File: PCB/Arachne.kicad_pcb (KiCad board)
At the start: 2 copper layers, 100 x 100 mm, 276 parts, among them J201 SW2, J301 SW2, J401 SW2, J501 SW2, J601 SW2, J701 SW2, J801 V_IN, J901 USB_B, J902 PROG_CONN_STM_6p, J903 DBG_UART, M201 Stepper_Motor_bipolar, M301 Stepper_Motor_bipolar, M401 Stepper_Motor_bipolar, M501 Stepper_Motor_bipolar, M601 Stepper_Motor_bipolar, M701 Stepper_Motor_bipolar, Q801 AOD4189, SW101 SW_Push, U101 STM32L452CEUx, U102 WS2818B, U201 L6470_HTSSOP28, U301 L6470_HTSSOP28, U401 L6470_HTSSOP28, U501 L6470_HTSSOP28, U601 L6470_HTSSOP28, U701 L6470_HTSSOP28, U801 ACS712xLCTR-20A, U802 NCP1117-5.0_SOT223, U803 L5973D, U804 NCP1117-3.3_SOT223, U901 USBLC6-2SC6

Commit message: PCB: component sorting, add driver space marks to comment layer
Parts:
- moved J903 174.8 mm to (192.0, 60.0)
- moved U101 169.4 mm to (150.0, 73.0)
- moved C708 117.1 mm to (219.0, 153.0)
- moved R701 117.0 mm to (219.0, 143.0)
- moved C704 116.5 mm to (228.0, 143.0)
- moved C712 114.7 mm to (219.0, 148.0)
- moved R705 114.6 mm to (228.0, 148.0)
- moved C701 112.7 mm to (228.0, 153.0)
- moved C706 110.9 mm to (238.0, 143.0)
- moved C709 109.1 mm to (238.0, 148.0)
- moved R704 107.9 mm to (246.0, 143.0)
- moved C802 105.5 mm to (133.0, 62.5)
- moved R702 102.5 mm to (238.0, 153.0)
- moved C713 102.4 mm to (246.0, 148.0)
- moved D702 102.4 mm to (267.0, 143.0)
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
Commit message: PCB: routing of first part of stepper motor driver
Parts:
- C701, C702, C703, C712, C713, D701, D702, D703, D704, D705, D706, D707, D708, D709, R701, R702, R703, R704, R705: moved to B.Cu
- moved U804 122.6 mm to (157.0, 41.6), turned to 90 degrees
- moved L801 103.2 mm to (116.3, 77.2), turned to 180 degrees
- moved U802 100.2 mm to (148.2, 42.2), turned to 90 degrees
- moved Q801 98.0 mm to (113.5, 64.0)
- moved D804 95.9 mm to (125.1, 80.0)
- moved RV801 91.3 mm to (131.0, 70.2)
- moved D805 87.7 mm to (125.1, 75.5), turned to 180 degrees
- moved U801 87.2 mm to (115.3, 70.2)
- moved U803 87.0 mm to (123.5, 70.2), turned to 180 degrees
- moved D709 86.9 mm to (181.2, 132.8), turned to 90 degrees
- moved D703 84.4 mm to (183.4, 137.2), turned to 90 degrees
- moved D705 81.7 mm to (181.2, 137.2), turned to 90 degrees
- moved R809 79.4 mm to (125.0, 62.6)
- moved C810 76.4 mm to (125.0, 66.4), turned to 180 degrees
- moved D707 76.3 mm to (185.8, 137.2), turned to 270 degrees
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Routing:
- net VMOT: track 0.00 -> 67.3 mm, vias 0 -> 2
- net +3V3: track 0.00 -> 38.5 mm, vias 0 -> 3
- net Net-(D705-Pad2): track 0.00 -> 34.4 mm, vias 0 -> 1
- net Net-(D704-Pad2): track 0.00 -> 29.3 mm, vias 0 -> 1
- net Net-(D702-Pad2): track 0.00 -> 17.9 mm, vias 0 -> 1
- net Net-(D703-Pad2): track 0.00 -> 17.6 mm, vias 0 -> 1
- net /Motor_1/MISO: track 0.00 -> 17.3 mm, vias 0 -> 1
- net /Motor_1/MOSI: track 0.00 -> 14.4 mm, vias 0 -> 1
- net /Motor_1/SCK: track 0.00 -> 14.3 mm, vias 0 -> 1
- net Net-(C712-Pad2): track 0.00 -> 13.0 mm, vias 0 -> 1
- net /BUSY_6: track 0.00 -> 11.6 mm, vias 0 -> 1
- net Net-(R703-Pad2): track 0.00 -> 10.8 mm, vias 0 -> 1
- net Net-(C701-Pad1): track 0.00 -> 10.6 mm, vias 0 -> 1
- net /FLAG_6: track 0.00 -> 8.30 mm, vias 0 -> 1
- net Net-(C713-Pad1): track 0.00 -> 7.30 mm
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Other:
- net class Default: clearance 0.2 -> 0.145; trace_width 0.25 -> 0.15; via_dia 0.8 -> 0.6; via_drill 0.4 -> 0.3
- rule trace_clearance: 0.2 -> 0.145
- rule trace_min: 0.2 -> 0.15
- rule via_min_size: 0.4 -> 0.6

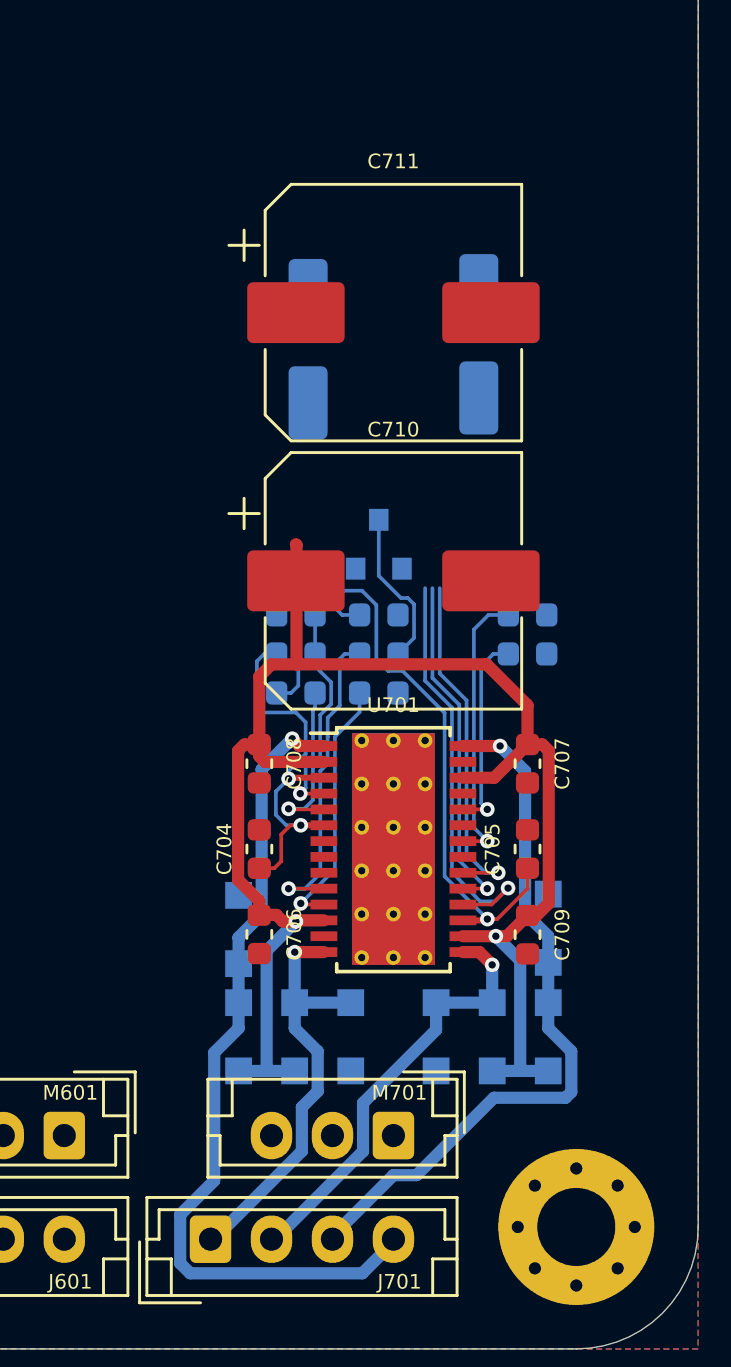
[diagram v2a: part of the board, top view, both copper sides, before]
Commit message: PCB: driver layout optimization, connect caps, connect endstop
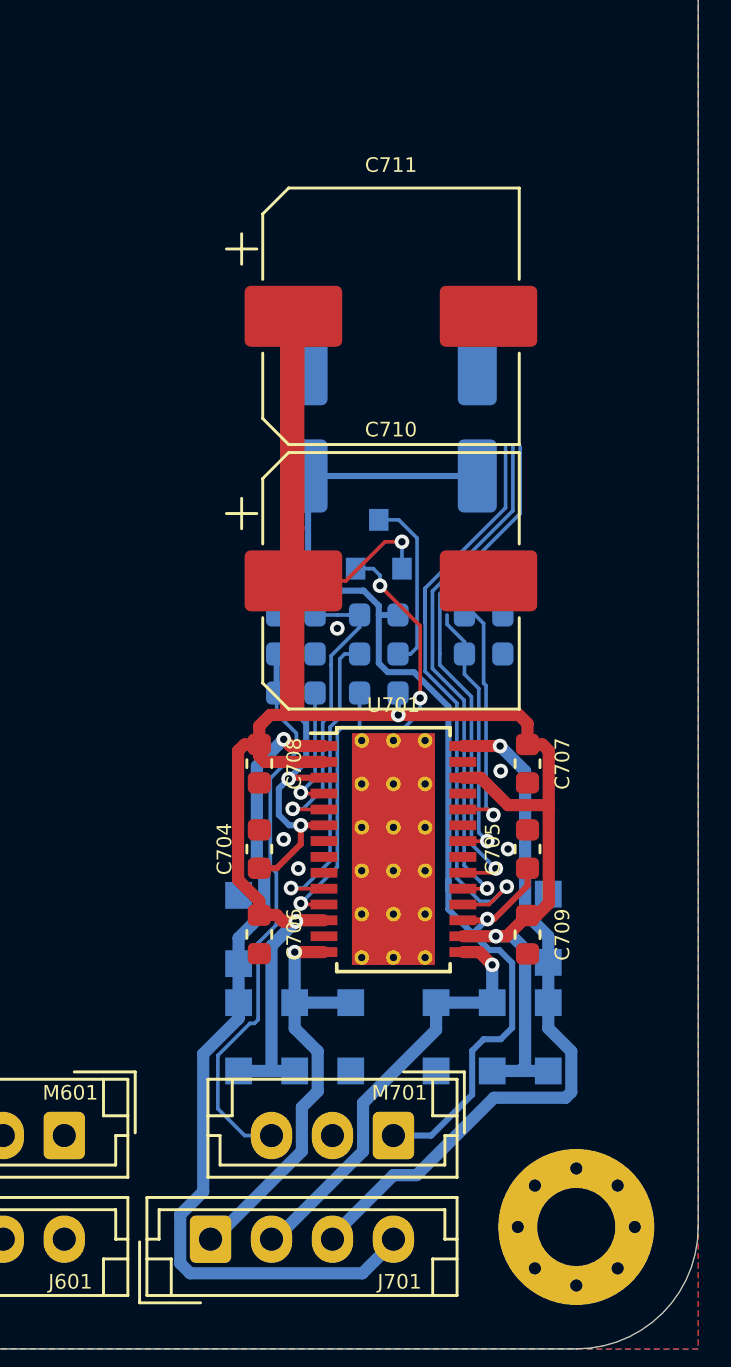
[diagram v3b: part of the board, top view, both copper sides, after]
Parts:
- moved C713 3.76 mm to (183.5, 121.5)
- moved R703 3.76 mm to (186.9, 119.9), turned to 180 degrees
- moved C702 3.20 mm to (190.9, 112.0)
- moved C703 3.00 mm to (184.0, 112.0)
- moved R701 2.41 mm to (191.2, 119.9)
- moved R702 2.41 mm to (191.2, 121.5)
- moved C711 0.18 mm to (187.4, 107.7)
- moved C710 0.10 mm to (187.4, 118.5)
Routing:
- net +3V3: track 38.5 -> 66.2 mm
- net VMOT: track 67.3 -> 83.5 mm, vias 2 -> 4
- net Net-(C713-Pad1): track 7.30 -> 23.3 mm
- net Net-(C701-Pad1): track 10.6 -> 21.2 mm, vias 1 -> 3
- net /Motor_1/MISO: track 17.3 -> 25.8 mm
- net /Motor_1/SCK: track 14.3 -> 21.4 mm
- net /Motor_1/MOSI: track 14.4 -> 21.0 mm
- net /FLAG_6: track 8.30 -> 10.3 mm
- net Net-(R703-Pad2): track 10.8 -> 12.4 mm
- net Net-(C712-Pad1): track 6.53 -> 7.25 mm
- net /BUSY_6: track 11.6 -> 11.0 mm
- net GND: vias 0 -> 5

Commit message: PCB: route CS track of 6th driver, optimize layout of driver, connect GND
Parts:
- moved D202 282.2 mm to (-34.3, -32.7), turned to 270 degrees
- moved D209 276.9 mm to (-34.3, -27.3), turned to 270 degrees
- moved C213 272.9 mm to (-34.8, -22.5), turned to 270 degrees
- moved C211 270.0 mm to (-26.7, -28.2), turned to 270 degrees
- moved C212 269.1 mm to (-34.8, -18.5), turned to 270 degrees
- moved C613 268.3 mm to (-15.8, 247.0), turned to 270 degrees
- moved C607 267.5 mm to (-27.0, 235.4), turned to 270 degrees
- moved C609 267.1 mm to (-20.5, 241.5), turned to 270 degrees
- moved C608 266.9 mm to (-13.3, 247.9), turned to 270 degrees
- moved R204 265.5 mm to (-34.8, -14.5), turned to 270 degrees
- moved C601 265.3 mm to (-29.0, 231.0), turned to 270 degrees
- moved C606 264.9 mm to (-24.5, 235.4), turned to 270 degrees
- moved R601 264.6 mm to (-10.8, 247.9), turned to 270 degrees
- moved R602 264.1 mm to (-15.8, 243.0), turned to 270 degrees
- moved R603 263.0 mm to (-20.5, 237.5), turned to 270 degrees
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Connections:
- C804 pad 1: /Power/MAIN_V_MON -> /PWR_MON
- C805 pad 1: /Power/I_MON -> /I_MON
- C808 pad 1: /Power/5V_MON -> /5V_MON
- D802 pad 1: (no net) -> /PWR_MON
- D802 pad 4: /Power/5V_MON -> /5V_MON
- D802 pad 6: /Power/I_MON -> /I_MON
- R301 pad 2: /Motor_2/FLAG -> /FLAG_2
- R302 pad 2: /Motor_2/BUSY -> /BUSY_2
- R801 pad 2: /Power/MAIN_V_MON -> /PWR_MON
- R802 pad 2: /Power/I_MON -> /I_MON
- R804 pad 1: /Power/MAIN_V_MON -> /PWR_MON
- R805 pad 1: /Power/I_MON -> /I_MON
- R806 pad 2: /Power/5V_MON -> /5V_MON
- R807 pad 1: /Power/5V_MON -> /5V_MON
- RN101 pad 7: (no net) -> /FLAG_2
- RN101 pad 8: (no net) -> /BUSY_2
- TP805 pad 1: /Power/I_MON -> /I_MON
- U101 pad 10: (no net) -> /5V_MON
- U101 pad 14: (no net) -> /BUSY_6
- U101 pad 15: (no net) -> /PWR_MON
- U101 pad 16: (no net) -> /I_MON
- U101 pad 18: (no net) -> /FLAG_1
- U101 pad 19: (no net) -> /FLAG_2
- U101 pad 2: (no net) -> /BUSY_4
- U101 pad 20: (no net) -> /FLAG_3
- U101 pad 21: (no net) -> /CS_4
- U101 pad 22: (no net) -> /CS_5
- U101 pad 25: (no net) -> /CS_6
- U101 pad 3: (no net) -> /BUSY_5
- U101 pad 39: (no net) -> /FLAG_4
- U101 pad 41: (no net) -> /FLAG_5
- U101 pad 42: (no net) -> /FLAG_6
- U101 pad 43: (no net) -> /CS_1
- U101 pad 44: (no net) -> /BUSY_3
- U101 pad 45: (no net) -> /CS_2
- U101 pad 46: (no net) -> /CS_3
- U101 pad 5: (no net) -> /BUSY_1
- U101 pad 6: (no net) -> /BUSY_2
- U201 pad 18: /Motor_1/MISO -> /SPI_MISO
- U201 pad 19: /Motor_1/SCK -> /SPI_SCK
- U201 pad 20: /Motor_1/MOSI -> /SPI_MOSI
- U201 pad 23: (no net) -> /CS_1
- U301 pad 18: /Motor_1/MISO -> /SPI_MISO
- U301 pad 19: /Motor_1/SCK -> /SPI_SCK
- U301 pad 20: /Motor_1/MOSI -> /SPI_MOSI
- U301 pad 22: /Motor_2/BUSY -> /BUSY_2
- U301 pad 23: (no net) -> /CS_2
- U301 pad 24: /Motor_2/FLAG -> /FLAG_2
- U401 pad 18: /Motor_1/MISO -> /SPI_MISO
- U401 pad 19: /Motor_1/SCK -> /SPI_SCK
- U401 pad 20: /Motor_1/MOSI -> /SPI_MOSI
- U401 pad 23: (no net) -> /CS_3
- U501 pad 18: /Motor_1/MISO -> /SPI_MISO
- U501 pad 19: /Motor_1/SCK -> /SPI_SCK
- U501 pad 20: /Motor_1/MOSI -> /SPI_MOSI
- U501 pad 23: (no net) -> /CS_4
- U601 pad 18: /Motor_1/MISO -> /SPI_MISO
- U601 pad 19: /Motor_1/SCK -> /SPI_SCK
- U601 pad 20: /Motor_1/MOSI -> /SPI_MOSI
- U601 pad 23: (no net) -> /CS_5
- U701 pad 18: /Motor_1/MISO -> /SPI_MISO
- U701 pad 19: /Motor_1/SCK -> /SPI_SCK
- U701 pad 20: /Motor_1/MOSI -> /SPI_MOSI
- U701 pad 23: (no net) -> /CS_6
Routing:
- net /Motor_1/MISO: track 25.8 -> 0.00 mm, vias 1 -> 0
- net /SPI_MISO: track 0.00 -> 25.8 mm, vias 0 -> 1
- net /CS_6: track 0.00 -> 22.0 mm, vias 0 -> 1
- net /SPI_MOSI: track 0.00 -> 21.4 mm, vias 0 -> 1
- net /SPI_SCK: track 0.00 -> 21.4 mm, vias 0 -> 1
- net /Motor_1/SCK: track 21.4 -> 0.00 mm, vias 1 -> 0
- net /Motor_1/MOSI: track 21.0 -> 0.00 mm, vias 1 -> 0
- net +3V3: track 66.2 -> 78.7 mm, vias 3 -> 5
- net /FLAG_6: track 10.3 -> 18.8 mm
- net /BUSY_6: track 11.0 -> 19.4 mm
- net Net-(D704-Pad2): track 29.3 -> 30.7 mm
- net VMOT: track 83.5 -> 82.7 mm
- net Net-(C712-Pad1): track 7.25 -> 7.95 mm
- net GND: vias 5 -> 21
